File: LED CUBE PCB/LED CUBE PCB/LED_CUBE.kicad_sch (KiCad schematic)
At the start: 7 parts, among them J2 Conn_01x02

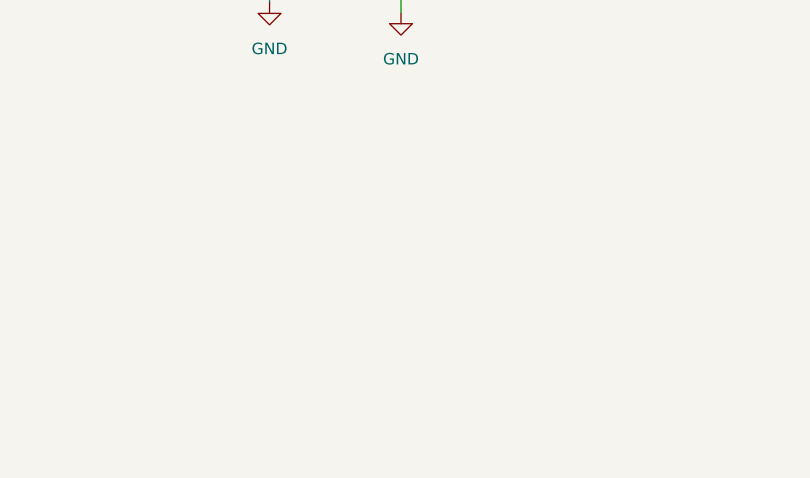
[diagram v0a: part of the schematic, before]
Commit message: Added header and global labels
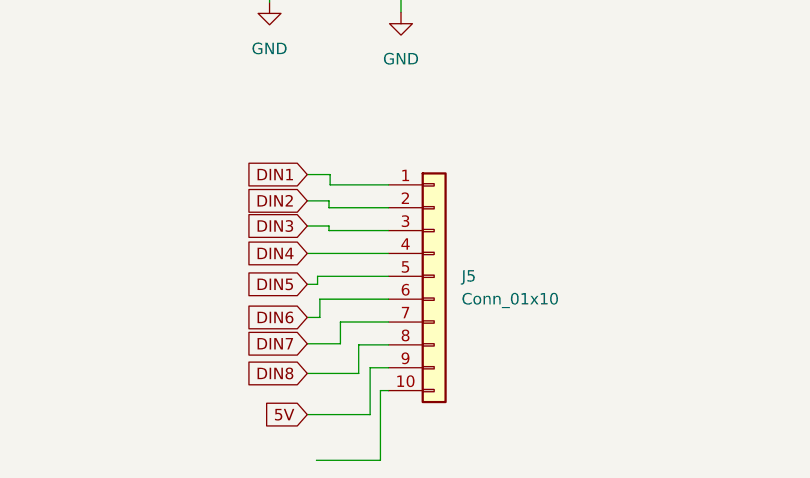
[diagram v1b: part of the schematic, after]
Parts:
- added J5: Conn_01x10, symbol Connector_Generic:Conn_01x10
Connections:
- net 5V: now also J5.9 (Pin_9)
- net DIN1: now also J5.1 (Pin_1)
- net DIN2: now also J5.2 (Pin_2)
- net DIN3: now also J5.3 (Pin_3)
- net DIN4: now also J5.4 (Pin_4)
- net DIN5: now also J5.5 (Pin_5)
- net DIN6: now also J5.6 (Pin_6)
- net DIN7: now also J5.7 (Pin_7)
- net DIN8: now also J5.8 (Pin_8)
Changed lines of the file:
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@@
+    (stroke (width 0) (type default))
+  )
+  (wire (pts (xy 145.415 87.503) (xy 145.415 86.36))
     (stroke (width 0) (type default))
   )
@@
     (stroke (width 0) (type default))
   )
+  (wire (pts (xy 142.875 95.123) (xy 151.892 95.123))
+    (stroke (width 0) (type default))
+  )
   (wire (pts (xy 59.055 61.722) (xy 59.055 62.611))
     (stroke (width 0) (type default))
@@
     (stroke (width 0) (type default))
   )
+  (wire (pts (xy 151.892 97.663) (xy 144.018 97.663))
+    (stroke (width 0) (type default))
+  )
   (wire (pts (xy 88.9 69.596) (xy 94.361 69.596))
     (stroke (width 0) (type default))
@@
     (stroke (width 0) (type default))
   )
+  (wire (pts (xy 145.415 87.503) (xy 151.892 87.503))
+    (stroke (width 0) (type default))
+  )
+  (wire (pts (xy 151.892 110.363) (xy 151.003 110.363))
+    (stroke (width 0) (type default))
+  )
   (wire (pts (xy 67.437 61.722) (xy 59.055 61.722))
     (stroke (width 0) (type default))
   )
+  (wire (pts (xy 142.875 86.36) (xy 145.415 86.36))
+    (stroke (width 0) (type default))
+  )
   (wire (pts (xy 55.245 57.277) (xy 67.437 57.277))
     (stroke (width 0) (type default))
@@
     (stroke (width 0) (type default))
   )
+  (wire (pts (xy 142.875 105.156) (xy 146.558 105.156))
+    (stroke (width 0) (type default))
+  )
   (wire (pts (xy 39.624 83.566) (xy 45.466 83.566))
     (stroke (width 0) (type default))
   )
+  (wire (pts (xy 142.875 113.03) (xy 149.86 113.03))
+    (stroke (width 0) (type default))
+  )
   (wire (pts (xy 83.947 50.673) (xy 91.821 50.673))
     (stroke (width 0) (type default))
@@
     (stroke (width 0) (type default))
   )
+  (wire (pts (xy 151.892 100.203) (xy 144.272 100.203))
+    (stroke (width 0) (type default))
+  )
+  (wire (pts (xy 151.892 92.583) (xy 145.288 92.583))
+    (stroke (width 0) (type default))
+  )
   (wire (pts (xy 87.249 88.138) (xy 94.996 88.138))
     (stroke (width 0) (type default))
@@
     (stroke (width 0) (type default))
   )
+  (wire (pts (xy 149.86 107.823) (xy 149.86 113.03))
+    (stroke (width 0) (type default))
+  )
   (wire (pts (xy 57.658 51.054) (xy 57.658 52.832))
     (stroke (width 0) (type default))
@@
     (stroke (width 0) (type default))
   )
+  (wire (pts (xy 144.018 97.663) (xy 144.018 98.552))
+    (stroke (width 0) (type default))
+  )
   (wire (pts (xy 54.737 101.473) (xy 54.737 102.997))
     (stroke (width 0) (type default))
@@
     (stroke (width 0) (type default))
   )
+  (wire (pts (xy 151.892 90.043) (xy 145.288 90.043))
+    (stroke (width 0) (type default))
+  )
+  (wire (pts (xy 151.892 105.283) (xy 148.59 105.283))
+    (stroke (width 0) (type default))
+  )
   (wire (pts (xy 138.684 47.371) (xy 138.684 55.372))
     (stroke (width 0) (type default))
@@
     (stroke (width 0) (type default))
   )
+  (wire (pts (xy 142.875 102.235) (xy 144.272 102.235))
+    (stroke (width 0) (type default))
+  )
   (wire (pts (xy 92.71 60.452) (xy 93.98 60.452))
     (stroke (width 0) (type default))
@@
     (stroke (width 0) (type default))
   )
+  (wire (pts (xy 145.288 92.583) (xy 145.288 92.075))
+    (stroke (width 0) (type default))
+  )
   (wire (pts (xy 83.947 68.326) (xy 86.36 68.326))
     (stroke (width 0) (type default))
   )
+  (wire (pts (xy 151.892 102.743) (xy 146.558 102.743))
+    (stroke (width 0) (type default))
+  )
   (wire (pts (xy 53.467 43.942) (xy 60.96 43.942))
     (stroke (width 0) (type default))
@@
     (stroke (width 0) (type default))
   )
+  (wire (pts (xy 145.288 90.043) (xy 145.288 89.281))
+    (stroke (width 0) (type default))
+  )
+  (wire (pts (xy 146.558 102.743) (xy 146.558 105.156))
+    (stroke (width 0) (type default))
+  )
   (wire (pts (xy 90.297 43.942) (xy 94.107 43.942))
     (stroke (width 0) (type default))
   )
+  (wire (pts (xy 143.891 118.11) (xy 151.003 118.11))
+    (stroke (width 0) (type default))
+  )
   (wire (pts (xy 83.82 59.563) (xy 92.71 59.563))
     (stroke (width 0) (type default))
@@
     (stroke (width 0) (type default))
   )
+  (wire (pts (xy 142.875 98.552) (xy 144.018 98.552))
+    (stroke (width 0) (type default))
+  )
+  (wire (pts (xy 151.003 110.363) (xy 151.003 118.11))
+    (stroke (width 0) (type default))
+  )
   (wire (pts (xy 176.276 46.355) (xy 185.039 46.355))
     (stroke (width 0) (type default))
@@
     (stroke (width 0) (type default))
   )
+  (wire (pts (xy 148.59 108.458) (xy 148.59 105.283))
+    (stroke (width 0) (type default))
+  )
+  (wire (pts (xy 142.875 89.281) (xy 145.288 89.281))
+    (stroke (width 0) (type default))
+  )
+  (wire (pts (xy 142.875 92.075) (xy 145.288 92.075))
+    (stroke (width 0) (type default))
+  )
   (wire (pts (xy 63.373 66.04) (xy 67.437 66.04))
     (stroke (width 0) (type default))
@@
   )
   (wire (pts (xy 91.821 47.752) (xy 93.98 47.752))
+    (stroke (width 0) (type default))
+  )
+  (wire (pts (xy 142.875 108.458) (xy 148.59 108.458))
+    (stroke (width 0) (type default))
+  )
+  (wire (pts (xy 144.272 100.203) (xy 144.272 102.235))
+    (stroke (width 0) (type default))
+  )
+  (wire (pts (xy 149.86 107.823) (xy 151.892 107.823))
     (stroke (width 0) (type default))
   )
@@
     )
   )
+  (global_label "DIN7" (shape input) (at 142.875 105.156 180) (fields_autoplaced)
+    (effects (font (size 1.27 1.27)) (justify right))
+    (property "Intersheetrefs" "${INTERSHEET_REFS}" (at 135.475 105.156 0)
+      (effects (font (size 1.27 1.27)) (justify right) hide)
+    )
+  )
   (global_label "OE" (shape input) (at 61.087 59.436 180) (fields_autoplaced)
     (effects (font (size 1.27 1.27)) (justify right))
@@
     )
   )
+  (global_label "DIN6" (shape input) (at 142.875 102.235 180) (fields_autoplaced)
+    (effects (font (size 1.27 1.27)) (justify right))
+    (property "Intersheetrefs" "${INTERSHEET_REFS}" (at 135.475 102.235 0)
+      (effects (font (size 1.27 1.27)) (justify right) hide)
+    )
+  )
   (global_label "5V" (shape input) (at 176.276 46.355 180) (fields_autoplaced)
     (effects (font (size 1.27 1.27)) (justify right))
@@
     )
   )
+  (global_label "DIN3" (shape input) (at 142.875 92.075 180) (fields_autoplaced)
+    (effects (font (size 1.27 1.27)) (justify right))
+    (property "Intersheetrefs" "${INTERSHEET_REFS}" (at 135.475 92.075 0)
+      (effects (font (size 1.27 1.27)) (justify right) hide)
+    )
+  )
   (global_label "GND" (shape input) (at 93.98 60.452 0) (fields_autoplaced)
     (effects (font (size 1.27 1.27)) (justify left))
@@
     )
   )
+  (global_label "DIN2" (shape input) (at 142.875 89.281 180) (fields_autoplaced)
+    (effects (font (size 1.27 1.27)) (justify right))
+    (property "Intersheetrefs" "${INTERSHEET_REFS}" (at 135.475 89.281 0)
+      (effects (font (size 1.27 1.27)) (justify right) hide)
+    )
+  )
   (global_label "DIN7" (shape input) (at 94.361 69.596 0) (fields_autoplaced)
     (effects (font (size 1.27 1.27)) (justify left))
@@
     )
   )
+  (global_label "DIN1" (shape input) (at 142.875 86.36 180) (fields_autoplaced)
+    (effects (font (size 1.27 1.27)) (justify right))
+    (property "Intersheetrefs" "${INTERSHEET_REFS}" (at 135.475 86.36 0)
+      (effects (font (size 1.27 1.27)) (justify right) hide)
+    )
+  )
   (global_label "PB5" (shape input) (at 55.372 65.405 180) (fields_autoplaced)
     (effects (font (size 1.27 1.27)) (justify right))
@@
     )
   )
+  (global_label "5V" (shape input) (at 142.875 113.03 180) (fields_autoplaced)
+    (effects (font (size 1.27 1.27)) (justify right))
+    (property "Intersheetrefs" "${INTERSHEET_REFS}" (at 137.5917 113.03 0)
+      (effects (font (size 1.27 1.27)) (justify right) hide)
+    )
+  )
+  (global_label "DIN4" (shape input) (at 142.875 95.123 180) (fields_autoplaced)
+    (effects (font (size 1.27 1.27)) (justify right))
+    (property "Intersheetrefs" "${INTERSHEET_REFS}" (at 135.475 95.123 0)
+      (effects (font (size 1.27 1.27)) (justify right) hide)
+    )
+  )
   (global_label "DIN8" (shape input) (at 94.361 73.66 0) (fields_autoplaced)
     (effects (font (size 1.27 1.27)) (justify left))
@@
     (property "Intersheetrefs" "${INTERSHEET_REFS}" (at 153.289 43.1037 90)
       (effects (font (size 1.27 1.27)) (justify left) hide)
+    )
+  )
+  (global_label "DIN8" (shape input) (at 142.875 108.458 180) (fields_autoplaced)
+    (effects (font (size 1.27 1.27)) (justify right))
+    (property "Intersheetrefs" "${INTERSHEET_REFS}" (at 135.475 108.458 0)
+      (effects (font (size 1.27 1.27)) (justify right) hide)
+    )
+  )
+  (global_label "DIN5" (shape input) (at 142.875 98.552 180) (fields_autoplaced)
+    (effects (font (size 1.27 1.27)) (justify right))
+    (property "Intersheetrefs" "${INTERSHEET_REFS}" (at 135.475 98.552 0)
+      (effects (font (size 1.27 1.27)) (justify right) hide)
     )
   )
@@
         )
       )
+    )
+  )
+  (symbol (lib_id "Connector_Generic:Conn_01x10") (at 156.972 97.663 0) (unit 1)
+    (in_bom yes) (on_board yes) (dnp no) (fields_autoplaced)
+    (property "Reference" "J5" (at 160.02 97.663 0)
+      (effects (font (size 1.27 1.27)) (justify left))
+    )
+    (property "Value" "Conn_01x10" (at 160.02 100.203 0)
+      (effects (font (size 1.27 1.27)) (justify left))
+    )
+    (property "Footprint" "" (at 156.972 97.663 0)
+      (effects (font (size 1.27 1.27)) hide)
+    )
+    (property "Datasheet" "~" (at 156.972 97.663 0)
+      (effects (font (size 1.27 1.27)) hide)
+    )
+    (pin "1")
+    (pin "10")
+    (pin "2")
+    (pin "3")
+    (pin "4")
+    (pin "5")
+    (pin "6")
+    (pin "7")
+    (pin "8")
+    (pin "9")
+    (instances
+      (project "LED CUBE PCB"
+        (path "/64eb2d32-222b-4351-90b6-2cc90b760e62/5690a520-fa1c-482f-a977-8101e9fd3d41"
+          (reference "J5") (unit 1)
+        )
+      )

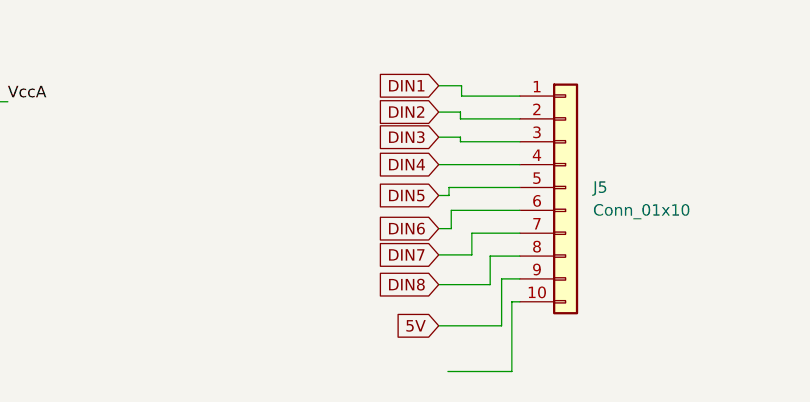
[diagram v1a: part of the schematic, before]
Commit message: Added logic level converter
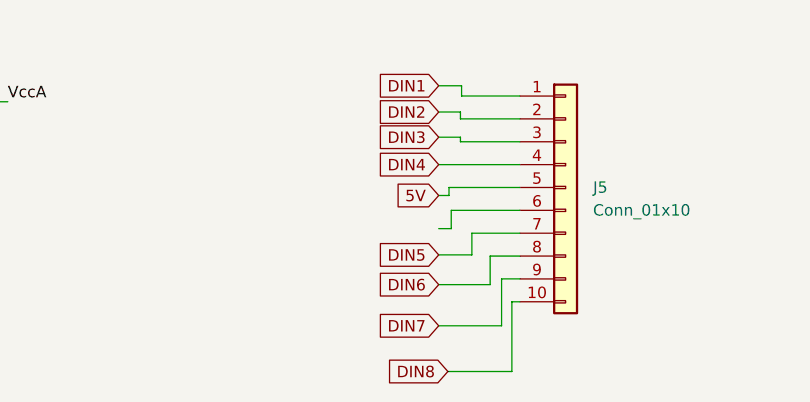
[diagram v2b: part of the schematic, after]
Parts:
- J5: footprint (none) -> Connector_PinSocket_2.54mm:PinSocket_1x10_P2.54mm_Vertical
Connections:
- net 5V: now also J5.5 (Pin_5); no longer J5.9 (Pin_9)
- net DIN5: now also J5.7 (Pin_7); no longer J5.5 (Pin_5)
- net DIN6: now also J5.8 (Pin_8); no longer J5.6 (Pin_6)
- net DIN7: now also J5.9 (Pin_9); no longer J5.7 (Pin_7)
- net DIN8: now also J5.10 (Pin_10); no longer J5.8 (Pin_8)
